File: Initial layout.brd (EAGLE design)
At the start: 153.3 x 128.3 mm, 32 parts, among them U2 TPS54540DDARQ1

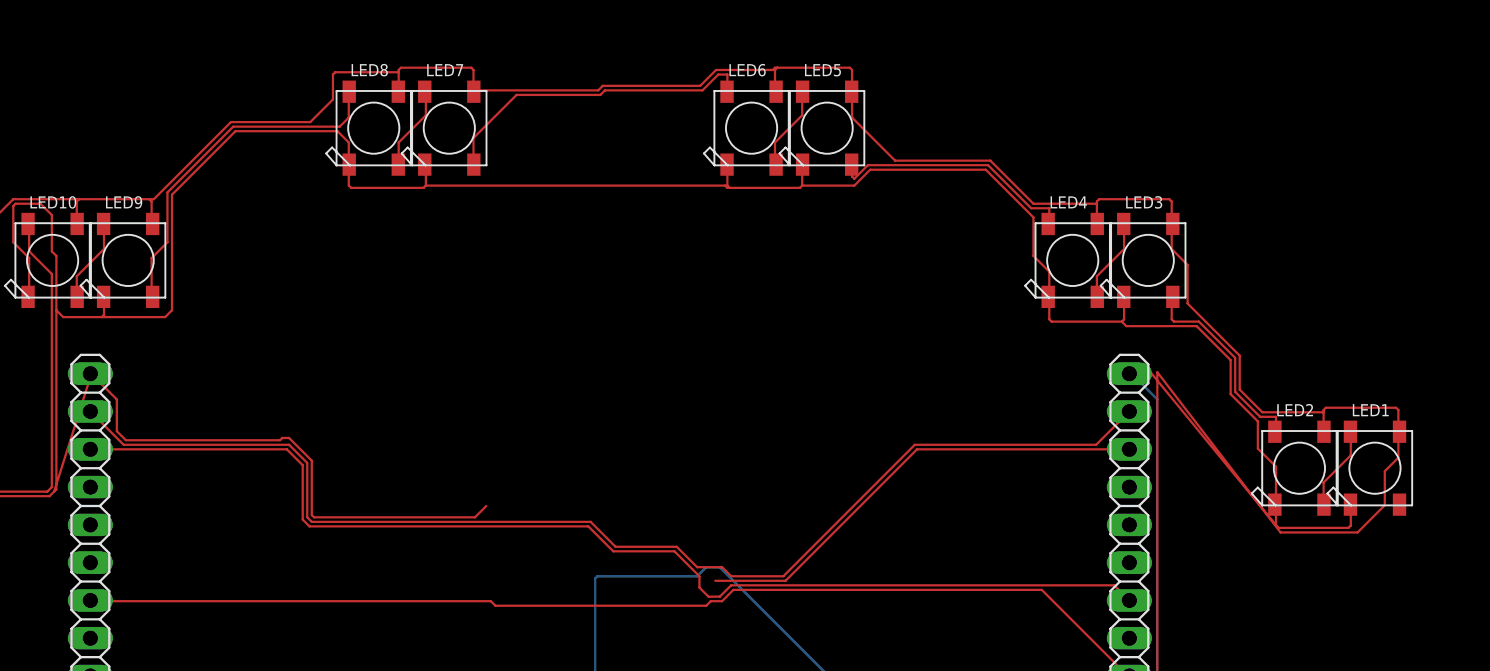
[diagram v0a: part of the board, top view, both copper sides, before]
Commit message: Worked on schematic. Connected some wires
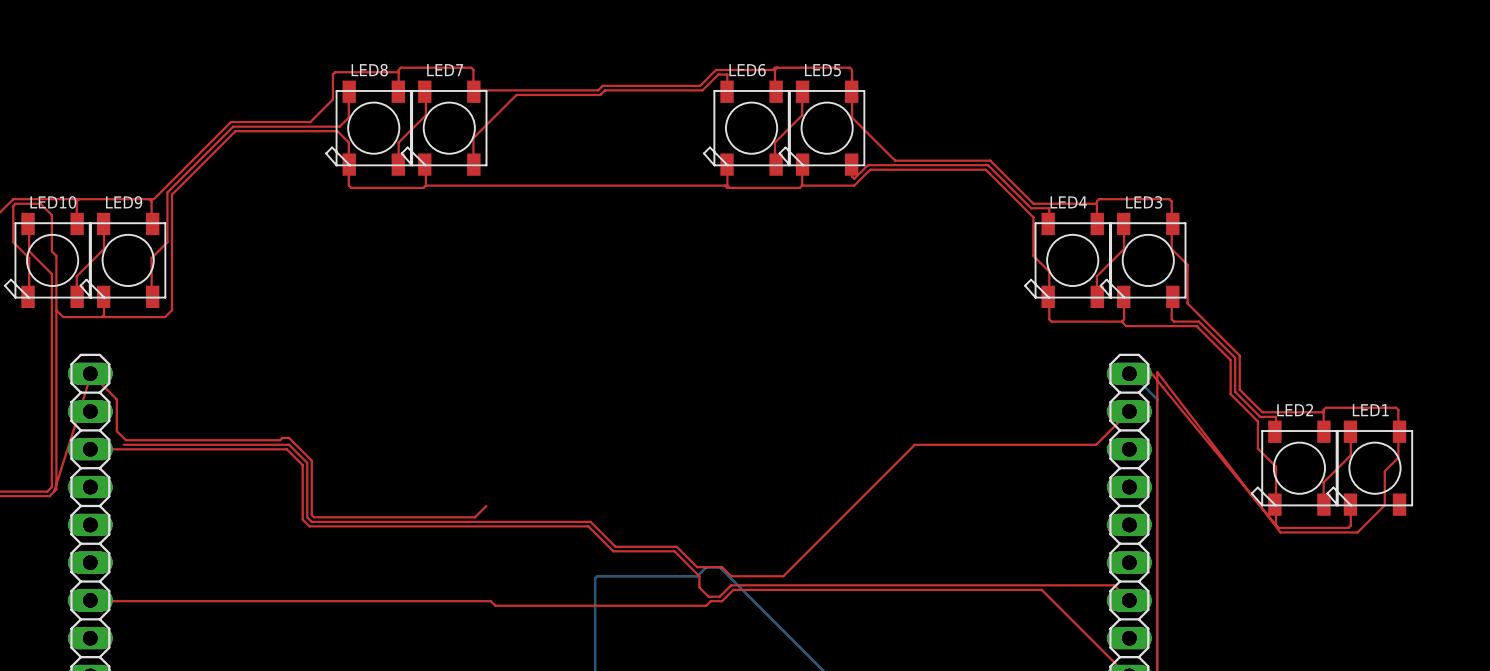
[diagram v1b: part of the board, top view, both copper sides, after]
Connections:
- removed net 3-5V: JP1.19, JP2.19
- removed net 3.3V: JP1.18
- new net N$1: LED2.3-GND
- net +5V: now also JP1.19
- net CLK: now also U$2.13/SCK
- net CS: now also U$2.10/CS
- net D/C: now also U$2.9/CS
- net GND: no longer LED2.3-GND
- net MISO: now also U$2.12/MISO; no longer U$2.11/MOSI
- net MOSI: now also U$2.11/MOSI; no longer U$2.12/MISO
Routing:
- net 3-5V: track 81.2 -> 0.00 mm
- net +5V: track 308.7 -> 386.3 mm
- net 3.3V: track 31.5 -> 0.00 mm
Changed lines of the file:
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@@
 <?xml version="1.0" encoding="utf-8"?>
 <!DOCTYPE eagle SYSTEM "eagle.dtd">
-<eagle version="8.5.0">
+<eagle version="8.4.1">
 <drawing>
 <settings>
@@
 <param name="checkRestrict" value="1"/>
 <param name="checkStop" value="0"/>
-<param name="checkValues" value="0"/>
 <param name="useDiameter" value="13"/>
 <param name="maxErrors" value="50"/>
@@
 <contactref element="JP2" pad="20"/>
 <contactref element="LED1" pad="3-GND"/>
-<contactref element="LED2" pad="3-GND"/>
 <contactref element="LED3" pad="3-GND"/>
 <contactref element="LED4" pad="3-GND"/>
@@
 <wire x1="-14.3256" y1="65.9892" x2="-14.478" y2="65.8368" width="0.1524" layer="1"/>
 <wire x1="-14.3256" y1="67.3608" x2="-14.3256" y2="65.9892" width="0.1524" layer="1"/>
-<wire x1="-19.3548" y1="67.3608" x2="-19.43" y2="67.4" width="0.1524" layer="1"/>
 <wire x1="-14.3256" y1="67.3608" x2="-14.35" y2="67.4" width="0.1524" layer="1"/>
 <wire x1="-27.7876" y1="76.3016" x2="-29.1592" y2="76.3016" width="0.1524" layer="1"/>
@@
 <wire x1="-29.4132" y1="79.4004" x2="-24.6888" y2="79.4004" width="0.1524" layer="1"/>
 <wire x1="-29.718" y1="79.7052" x2="-29.4132" y2="79.4004" width="0.1524" layer="1"/>
-<wire x1="-19.3548" y1="67.5132" x2="-19.43" y2="67.4" width="0.1524" layer="1"/>
 <wire x1="-27.3304" y1="42.4688" x2="-29.1592" y2="40.64" width="0.1524" layer="16"/>
 <wire x1="-27.3304" y1="74.4728" x2="-27.3304" y2="42.4688" width="0.1524" layer="16"/>
@@
 <contactref element="U$2" pad="GND"/>
 <wire x1="-75.6412" y1="12.2936" x2="-130.81" y2="-48.26" width="0" layer="19" extent="1-1"/>
-</signal>
-<signal name="3.3V">
-<contactref element="JP1" pad="18"/>
-<wire x1="-43.4848" y1="71.12" x2="-29.21" y2="71.12" width="0.1524" layer="1"/>
-<wire x1="-52.324" y1="62.2808" x2="-43.4848" y2="71.12" width="0.1524" layer="1"/>
-<wire x1="-57.0484" y1="62.2808" x2="-52.324" y2="62.2808" width="0.1524" layer="1"/>
+<wire x1="-19.3548" y1="67.5132" x2="-19.3548" y2="67.3608" width="0" layer="19" extent="1-1"/>
 </signal>
 <signal name="+15V">
@@
 <contactref element="C26" pad="1"/>
 <contactref element="R28" pad="2"/>
-<contactref element="LED1" pad="1-VDD"/>
 <contactref element="LED2" pad="1-VDD"/>
 <contactref element="LED3" pad="1-VDD"/>
 <contactref element="LED4" pad="1-VDD"/>
 <contactref element="LED5" pad="1-VDD"/>
-<contactref element="LED6" pad="1-VDD"/>
 <contactref element="LED7" pad="1-VDD"/>
 <contactref element="LED8" pad="1-VDD"/>
@@
 <wire x1="-11.1252" y1="72.39" x2="-11.1252" y2="73.7616" width="0.1524" layer="1"/>
 <wire x1="-16.1544" y1="72.39" x2="-16.13" y2="72.3" width="0.1524" layer="1"/>
-<wire x1="-11.1252" y1="72.39" x2="-11.05" y2="72.3" width="0.1524" layer="1"/>
 <wire x1="-53.0352" y1="96.6216" x2="-53.0352" y2="95.25" width="0.1524" layer="1"/>
 <wire x1="-52.8828" y1="96.774" x2="-53.0352" y2="96.6216" width="0.1524" layer="1"/>
@@
 <wire x1="-47.8536" y1="96.6216" x2="-48.006" y2="96.774" width="0.1524" layer="1"/>
 <wire x1="-47.8536" y1="95.25" x2="-47.8536" y2="96.6216" width="0.1524" layer="1"/>
-<wire x1="-53.0352" y1="95.25" x2="-52.96" y2="95.16" width="0.1524" layer="1"/>
 <wire x1="-47.8536" y1="95.25" x2="-47.88" y2="95.16" width="0.1524" layer="1"/>
 <wire x1="-31.3944" y1="87.7824" x2="-31.3944" y2="87.63" width="0.1524" layer="1"/>
@@
 <wire x1="-11.1252" y1="70.5612" x2="-12.0396" y2="69.6468" width="0.1524" layer="1"/>
 <wire x1="-11.1252" y1="72.2376" x2="-11.1252" y2="70.5612" width="0.1524" layer="1"/>
-<wire x1="-11.1252" y1="72.2376" x2="-11.05" y2="72.3" width="0.1524" layer="1"/>
 <wire x1="-64.9224" y1="95.25" x2="-73.152" y2="95.25" width="0.1524" layer="1"/>
 <wire x1="-64.6176" y1="95.5548" x2="-64.9224" y2="95.25" width="0.1524" layer="1"/>
@@
 <via x="-57.0484" y="18.9992" extent="1-16" drill="0.35"/>
 <via x="-45.6184" y="16.7132" extent="1-16" drill="0.35"/>
+<contactref element="JP1" pad="19"/>
+<wire x1="-85.6996" y1="71.4248" x2="-96.8248" y2="71.4248" width="0.1524" layer="1"/>
+<wire x1="-84.4804" y1="70.2056" x2="-85.6996" y2="71.4248" width="0.1524" layer="1"/>
+<wire x1="-84.4804" y1="66.548" x2="-84.4804" y2="70.2056" width="0.1524" layer="1"/>
+<wire x1="-84.1756" y1="66.2432" x2="-84.4804" y2="66.548" width="0.1524" layer="1"/>
+<wire x1="-65.4304" y1="66.2432" x2="-84.1756" y2="66.2432" width="0.1524" layer="1"/>
+<wire x1="-63.754" y1="64.5668" x2="-65.4304" y2="66.2432" width="0.1524" layer="1"/>
+<wire x1="-59.6392" y1="64.5668" x2="-63.754" y2="64.5668" width="0.1524" layer="1"/>
+<wire x1="-58.2676" y1="63.1952" x2="-59.6392" y2="64.5668" width="0.1524" layer="1"/>
+<wire x1="-56.5912" y1="63.1952" x2="-58.2676" y2="63.1952" width="0.1524" layer="1"/>
+<wire x1="-55.9816" y1="62.5856" x2="-56.5912" y2="63.1952" width="0.1524" layer="1"/>
+<wire x1="-52.4764" y1="62.5856" x2="-55.9816" y2="62.5856" width="0.1524" layer="1"/>
+<wire x1="-43.6372" y1="71.4248" x2="-52.4764" y2="62.5856" width="0.1524" layer="1"/>
+<wire x1="-31.4452" y1="71.4248" x2="-43.6372" y2="71.4248" width="0.1524" layer="1"/>
+<wire x1="-29.21" y1="73.66" x2="-31.4452" y2="71.4248" width="0.1524" layer="1"/>
+<contactref element="LED1" pad="1-VDD"/>
+<contactref element="LED6" pad="1-VDD"/>
+<wire x1="-11.1252" y1="72.2376" x2="-11.05" y2="72.3" width="0" layer="19" extent="1-1"/>
+<wire x1="-11.1252" y1="72.39" x2="-11.05" y2="72.3" width="0" layer="19" extent="1-1"/>
+<wire x1="-52.96" y1="95.16" x2="-53.0352" y2="95.25" width="0" layer="19" extent="1-1"/>
+<wire x1="-29.21" y1="73.66" x2="-27.3304" y2="76.3016" width="0" layer="19" extent="1-1"/>
 </signal>
 <signal name="CARD_DETECT">
@@
 <signal name="D/C">
 <contactref element="JP1" pad="13"/>
+<contactref element="U$2" pad="9/CS"/>
+<wire x1="-29.21" y1="58.42" x2="-105.41" y2="-48.26" width="0" layer="19" extent="1-1"/>
 </signal>
 <signal name="CS">
@@
 <wire x1="-30.226" y1="61.976" x2="-55.9816" y2="61.976" width="0.1524" layer="1"/>
 <wire x1="-29.21" y1="60.96" x2="-30.226" y2="61.976" width="0.1524" layer="1"/>
+<contactref element="U$2" pad="10/CS"/>
+<wire x1="-84.328" y1="65.9384" x2="-102.87" y2="-48.26" width="0" layer="19" extent="1-1"/>
 </signal>
 <signal name="MOSI">
 <contactref element="JP1" pad="15"/>
-<contactref element="U$2" pad="12/MISO"/>
-<wire x1="-29.21" y1="63.5" x2="-97.79" y2="-48.26" width="0" layer="19" extent="1-1"/>
+<contactref element="U$2" pad="11/MOSI"/>
+<wire x1="-29.21" y1="63.5" x2="-100.33" y2="-48.26" width="0" layer="19" extent="1-1"/>
 </signal>
 <signal name="MISO">
 <contactref element="JP1" pad="16"/>
-<contactref element="U$2" pad="11/MOSI"/>
-<wire x1="-29.21" y1="66.04" x2="-100.33" y2="-48.26" width="0" layer="19" extent="1-1"/>
+<contactref element="U$2" pad="12/MISO"/>
+<wire x1="-29.21" y1="66.04" x2="-97.79" y2="-48.26" width="0" layer="19" extent="1-1"/>
 </signal>
 <signal name="CLK">
 <contactref element="JP1" pad="17"/>
-</signal>
-<signal name="3-5V">
-<contactref element="JP1" pad="19"/>
-<contactref element="JP2" pad="19"/>
-<wire x1="-96.8248" y1="71.4248" x2="-99.06" y2="73.66" width="0.1524" layer="1"/>
-<wire x1="-85.6996" y1="71.4248" x2="-96.8248" y2="71.4248" width="0.1524" layer="1"/>
-<wire x1="-84.4804" y1="70.2056" x2="-85.6996" y2="71.4248" width="0.1524" layer="1"/>
-<wire x1="-84.4804" y1="66.548" x2="-84.4804" y2="70.2056" width="0.1524" layer="1"/>
-<wire x1="-84.1756" y1="66.2432" x2="-84.4804" y2="66.548" width="0.1524" layer="1"/>
-<wire x1="-65.4304" y1="66.2432" x2="-84.1756" y2="66.2432" width="0.1524" layer="1"/>
-<wire x1="-63.754" y1="64.5668" x2="-65.4304" y2="66.2432" width="0.1524" layer="1"/>
-<wire x1="-59.6392" y1="64.5668" x2="-63.754" y2="64.5668" width="0.1524" layer="1"/>
-<wire x1="-58.2676" y1="63.1952" x2="-59.6392" y2="64.5668" width="0.1524" layer="1"/>
-<wire x1="-56.5912" y1="63.1952" x2="-58.2676" y2="63.1952" width="0.1524" layer="1"/>
-<wire x1="-55.9816" y1="62.5856" x2="-56.5912" y2="63.1952" width="0.1524" layer="1"/>
-<wire x1="-52.4764" y1="62.5856" x2="-55.9816" y2="62.5856" width="0.1524" layer="1"/>
-<wire x1="-43.6372" y1="71.4248" x2="-52.4764" y2="62.5856" width="0.1524" layer="1"/>
-<wire x1="-31.4452" y1="71.4248" x2="-43.6372" y2="71.4248" width="0.1524" layer="1"/>
-<wire x1="-29.21" y1="73.66" x2="-31.4452" y2="71.4248" width="0.1524" layer="1"/>
+<contactref element="U$2" pad="13/SCK"/>
+<wire x1="-29.21" y1="68.58" x2="-97.79" y2="-33.02" width="0" layer="19" extent="1-1"/>
 </signal>
 <signal name="D7">
@@
 <wire x1="-113.9952" y1="69.9516" x2="-113.92" y2="69.94" width="0.1524" layer="1"/>
 </signal>
+<signal name="N$1">
+<contactref element="LED2" pad="3-GND"/>
+</signal>
 </signals>

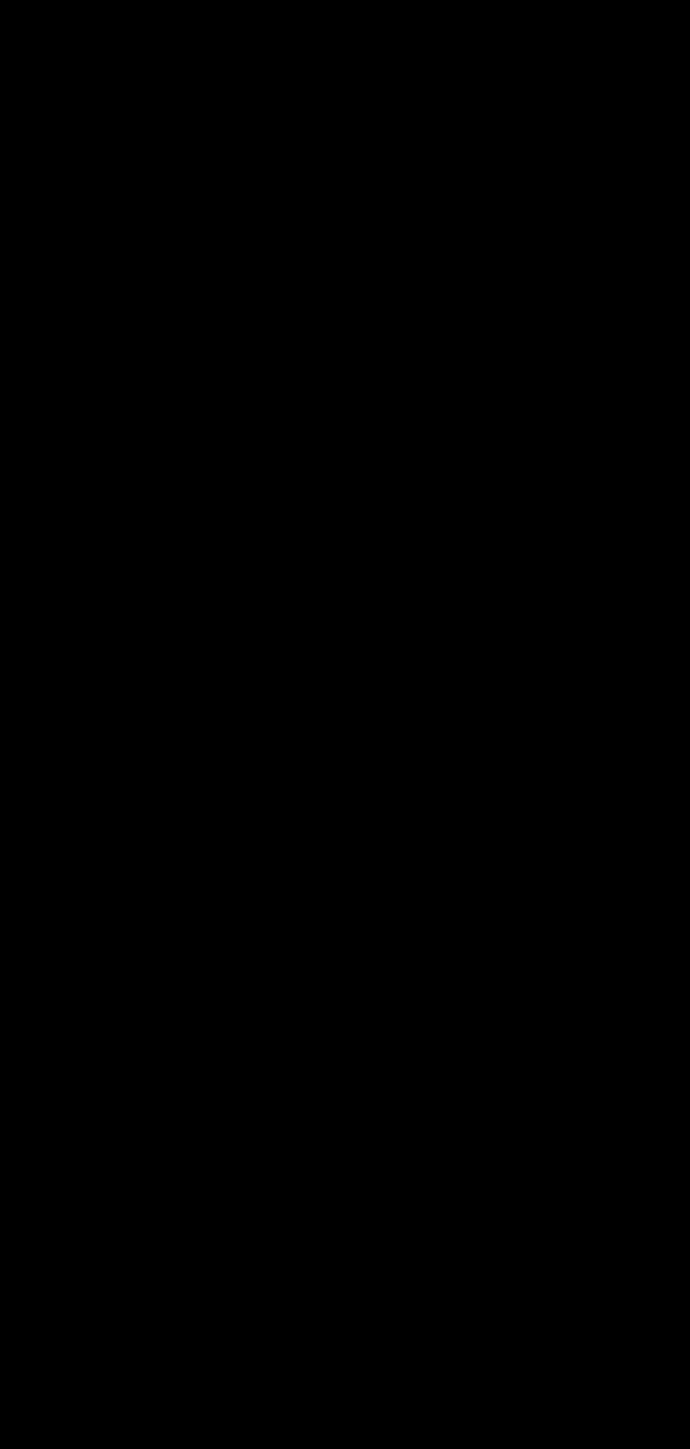
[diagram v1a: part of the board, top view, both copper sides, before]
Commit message: Added some connectors.
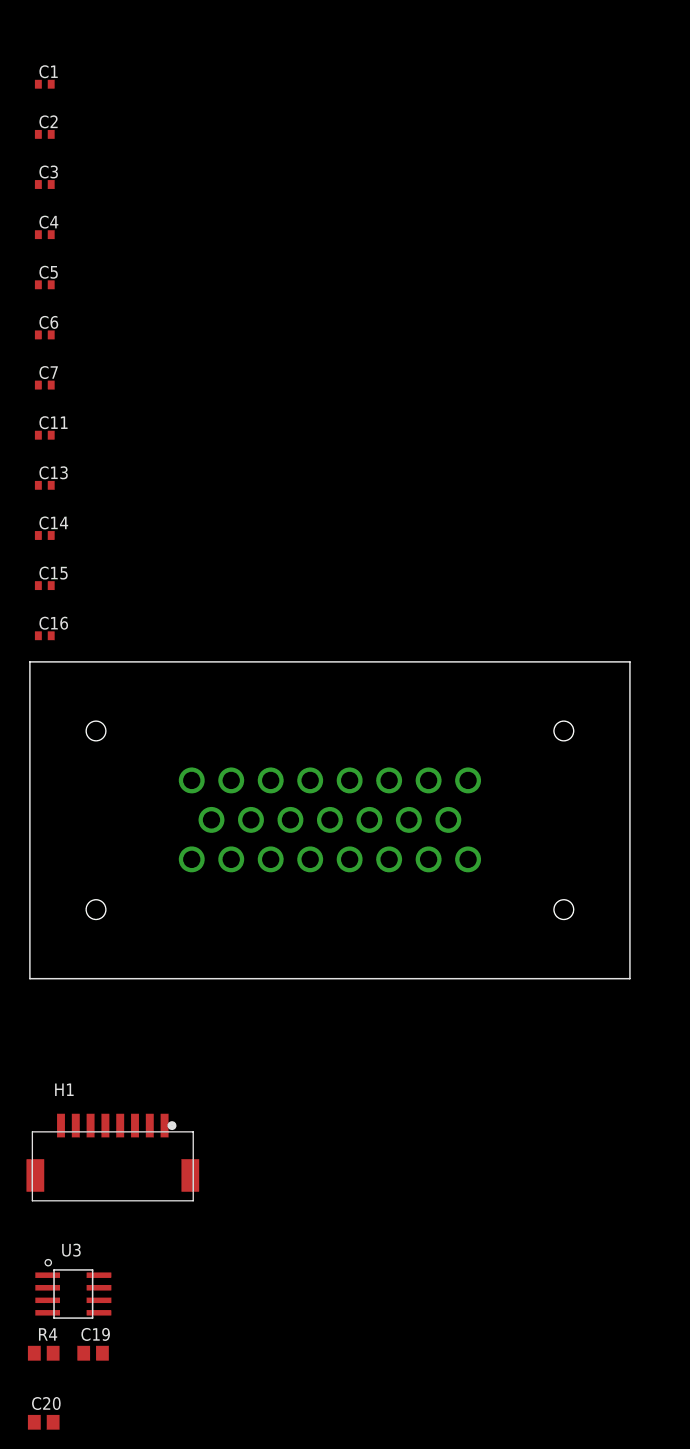
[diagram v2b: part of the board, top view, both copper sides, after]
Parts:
- added C1, C11, C13, C14, C15, C16, C2, C3, C4, C5, C6, C7: (no value), rcl:C0402
- added C19, C20: .1uF, rcl:C0805
- added H1: 5025840870, FormE:MOLEX-CLIKMATE-8-VERTICAL-HEADER
- added R4: 120, rcl:R0805
- added U$1: TE-776200-1, FormE:776200-1
- added U3: (no value), FormE:SOIC8-N_MC
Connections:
- new net +3V3: C20.1, H1.1, U$2.3V3, U3.5
- new net CANH1: R4.1, U$1.P$9, U3.7
- new net CANL1: R4.2, U$1.P$10, U3.6
- new net N$11: H1.2, U$2.24
- new net N$13: H1.3, U$2.25
- new net N$15: H1.4, U$2.26
- new net N$17: H1.5, U$2.27
- new net N$18: H1.6, U$2.28
- new net N$19: H1.7, U$2.29
- new net N$25: U$2.4/CANRX, U3.4
- new net N$26: U$2.3/CANTX, U3.1
- net +15V: now also U$1.P$1
- net +5V: now also C1.1, C11.1, C13.1, C14.1, C15.1, C16.1, C19.1, C2.1, C3.1, C4.1, C5.1, C6.1, C7.1, U$2.VIN, U3.3
- net GND: now also C1.2, C11.2, C13.2, C14.2, C15.2, C16.2, C19.2, C2.2, C20.2, C3.2, C4.2, C5.2, C6.2, C7.2, H1.8, U$1.P$16, U$2.GND3, U3.2, U3.8

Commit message: Gave Mike an Analog Line
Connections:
- removed net N$19: H1.7, U$2.29
- new net N$3: H1.7, U$2.31/A12
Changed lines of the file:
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@@
 <wire x1="-131.25" y1="-163.936" x2="-82.55" y2="-48.26" width="0" layer="19" extent="1-1"/>
-</signal>
-<signal name="N$19">
-<contactref element="U$2" pad="29"/>
-<contactref element="H1" pad="7"/>
-<wire x1="-132.75" y1="-163.936" x2="-80.01" y2="-48.26" width="0" layer="19" extent="1-1"/>
 </signal>
 <signal name="N$25">
@@
 <wire x1="-136.95" y1="-187" x2="-130.4" y2="-180.365" width="0" layer="19" extent="1-1"/>
 </signal>
+<signal name="N$3">
+<contactref element="H1" pad="7"/>
+<contactref element="U$2" pad="31/A12"/>
+<wire x1="-132.75" y1="-163.936" x2="-74.93" y2="-48.26" width="0" layer="19" extent="1-1"/>
+</signal>
 </signals>
